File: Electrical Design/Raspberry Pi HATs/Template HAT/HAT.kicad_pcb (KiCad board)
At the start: 2 copper layers, 65 x 30 mm, 14 parts, among them J1 CONN_02X01, J2 CONN_02X20, Q1 DMMT5401, Q2 DMG2305UX, U1 CAT24C32WI-GT3

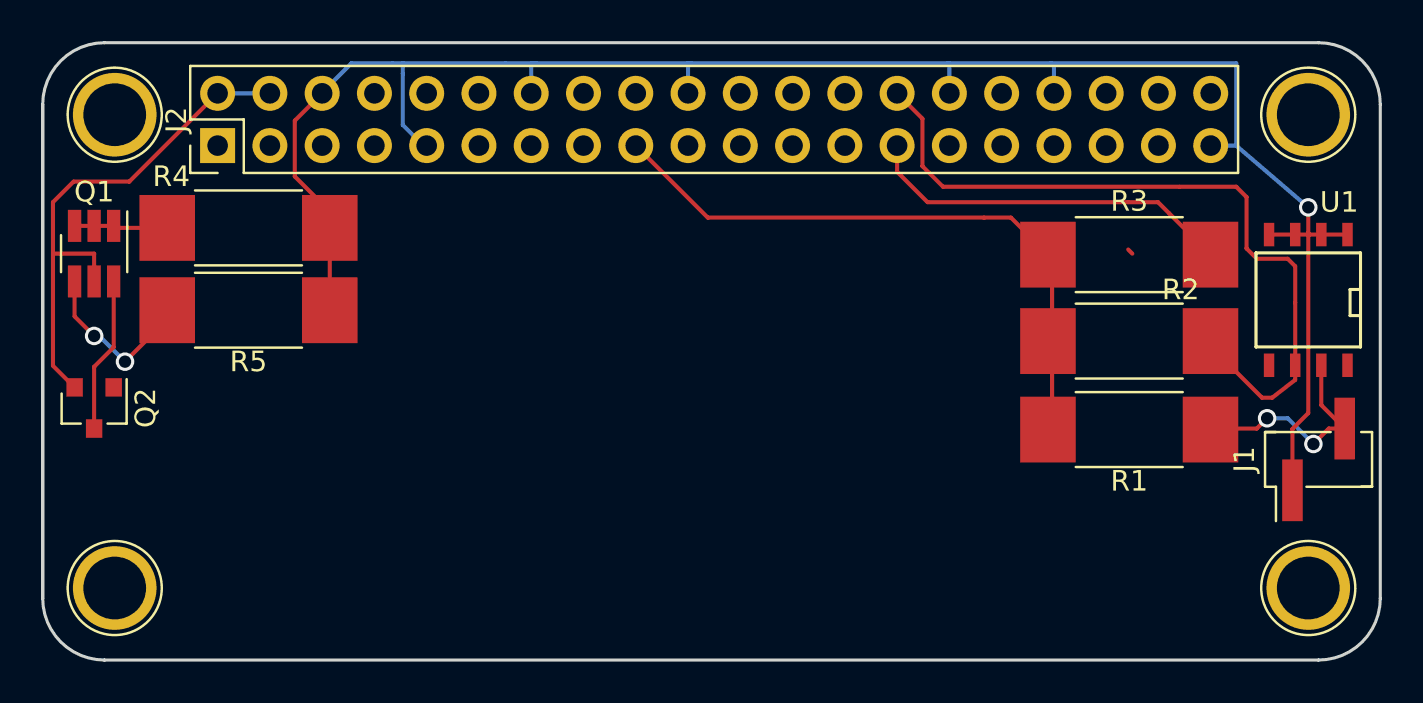
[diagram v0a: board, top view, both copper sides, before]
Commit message: Shrunk HAT template resistors
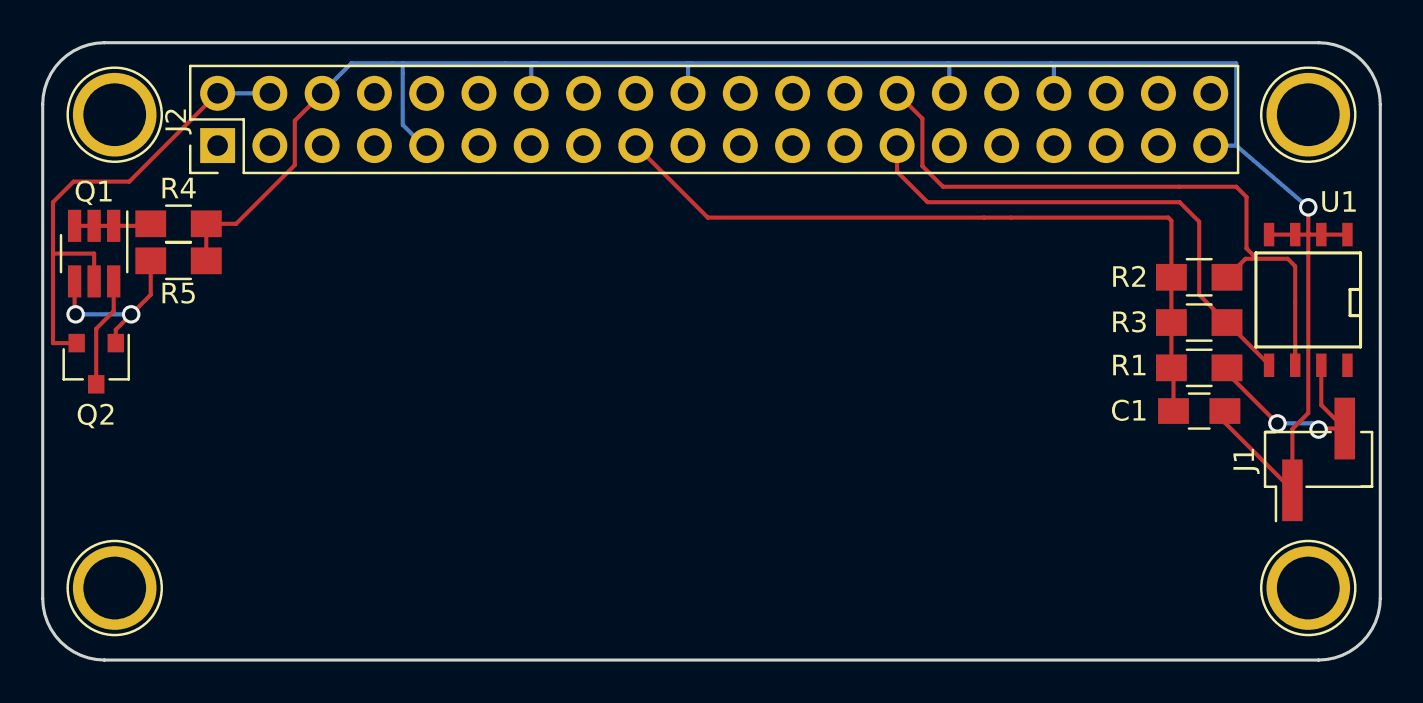
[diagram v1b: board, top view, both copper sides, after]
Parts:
- added C1: 100n, Capacitors_SMD:C_0805_HandSoldering, F.Cu at (236.2, 152.9)
- Q2: footprint TO_SOT_Packages_SMD:SOT-23 -> modules:SOT-23
- R1, R2, R3, R4, R5: footprint Resistors_SMD:R_2512_HandSoldering -> Resistors_SMD:R_0805_HandSoldering
- moved R3 4.74 mm to (236.2, 148.6)
- moved R2 4.60 mm to (236.2, 146.4)
- moved R1 4.53 mm to (236.2, 150.8)
- moved R5 4.16 mm to (186.6, 145.6)
- moved R4 3.41 mm to (186.6, 143.8)
- moved Q2 2.15 mm to (182.6, 150.6), turned to 180 degrees
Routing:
- net /Pi Connector/ID_SD: track 19.8 -> 25.3 mm
- net +3V3: track 31.4 -> 36.8 mm
- net GND: track 96.2 -> 101.1 mm
- net /Pi Connector/ID_SC: track 36.8 -> 32.3 mm
- net +5V: track 7.54 -> 5.35 mm
- net /Pi Connector/+5V_Pi: track 25.6 -> 24.1 mm
- net Net-(Q1-Pad1): track 4.54 -> 3.88 mm
- net Net-(Q1-Pad4): track 8.41 -> 9.02 mm

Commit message: Added I2C pullups to the HAT template for the device bus
Most boards (if not all) will use I2C for communication on the board.
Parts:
- added R6: 2.2K, Resistors_SMD:R_0805_HandSoldering, F.Cu at (191.5, 147.2)
- added R7: 2.2K, Resistors_SMD:R_0805_HandSoldering, F.Cu at (191.5, 145.5)
- added SCL: TEST, Pin_Headers:Pin_Header_Straight_1x01_Pitch2.54mm, F.Cu at (195.2, 147.8)
- added SDA: TEST, Pin_Headers:Pin_Header_Straight_1x01_Pitch2.54mm, F.Cu at (195.2, 145.0)
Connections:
- J2 pad 3: /Pi Connector/GPIO2 -> /SDA
- J2 pad 5: /Pi Connector/GPIO3 -> /SCL
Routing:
- net /SCL: track 0.00 -> 11.7 mm
- net /SDA: track 0.00 -> 10.8 mm, vias 0 -> 2
- net +3V3: track 36.8 -> 45.1 mm, vias 0 -> 2
- net GND: track 101.1 -> 108.5 mm, vias 1 -> 2
